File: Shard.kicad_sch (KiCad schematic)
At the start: 43 parts, among them J1 USB_C_Receptacle_USB2.0_16P, J2 Conn_01x02_Pin, SW1 SW_Push, SW2 SW_Push, U1 ESP32-S3, U2 USBLC6-2P6, U3 TLV76733DRVx, U4 TLV76733DRVx, U5 W25Q128JVS, Y1 Crystal_GND24_Small

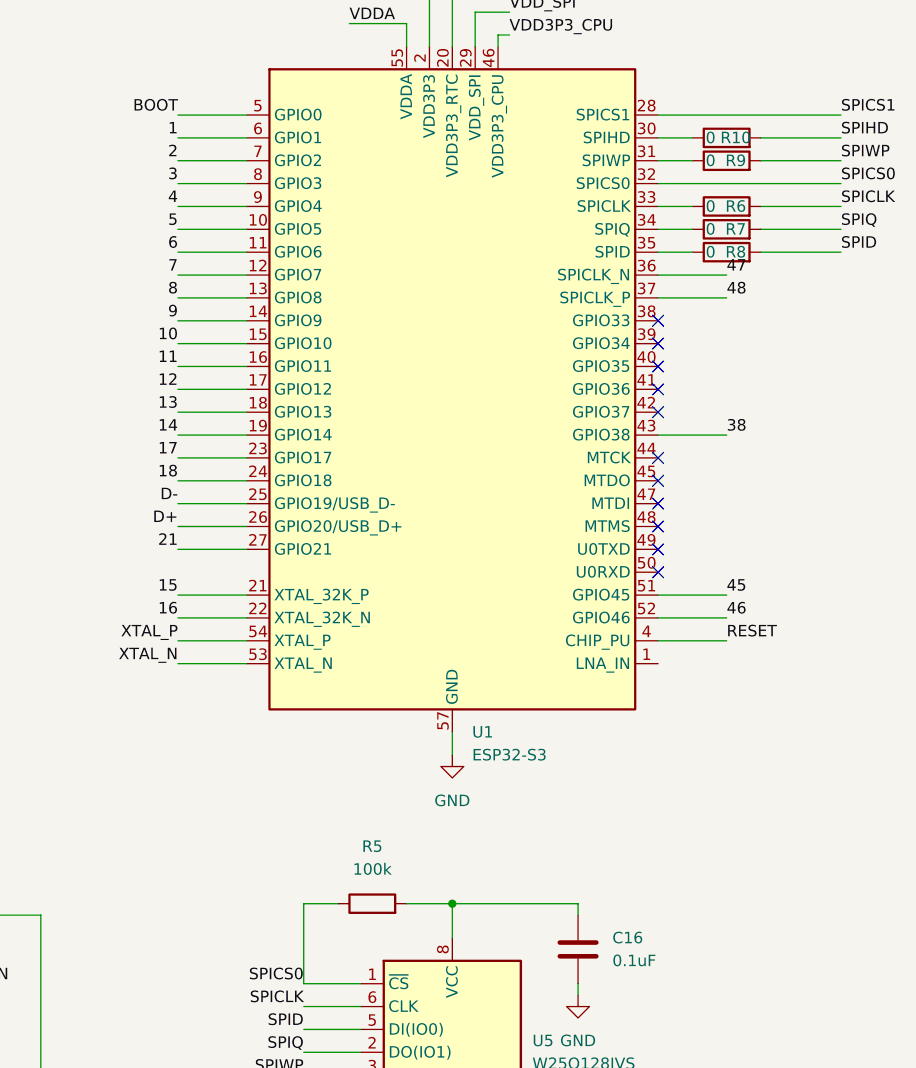
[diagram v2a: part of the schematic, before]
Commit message: GPIO pin labeling
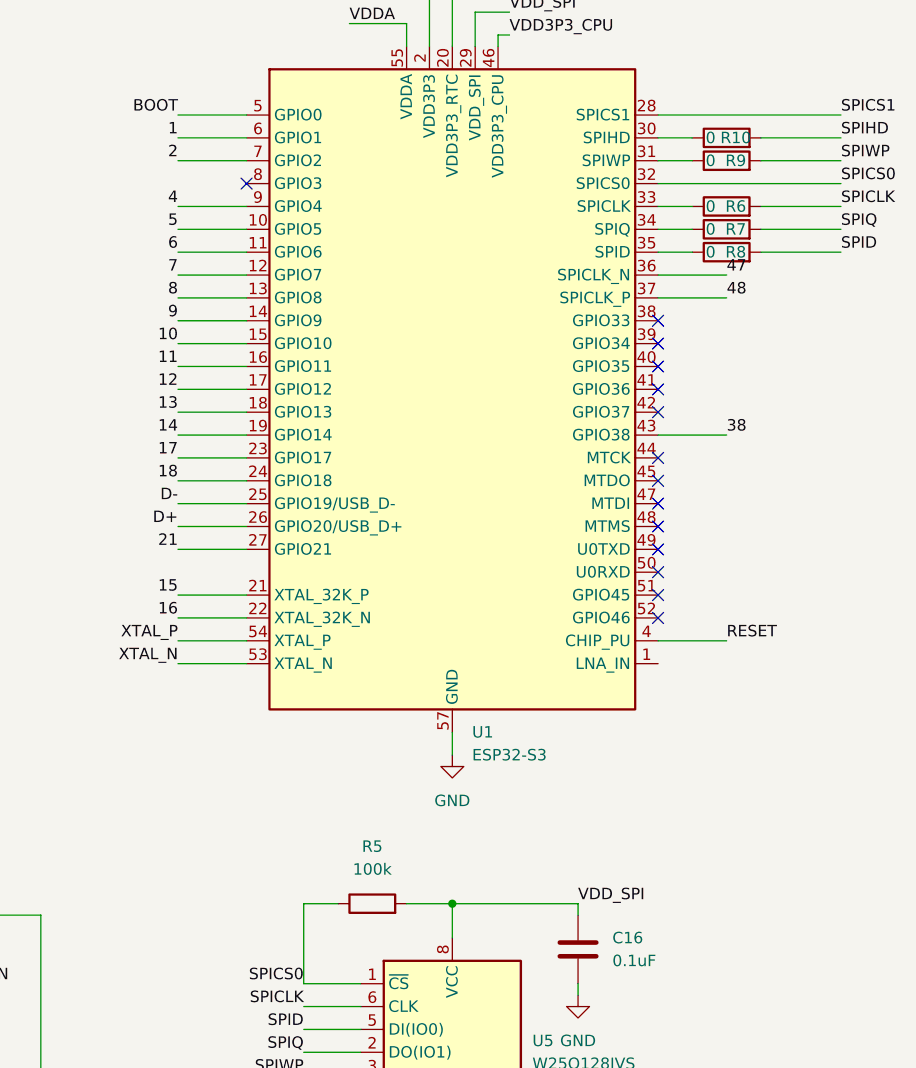
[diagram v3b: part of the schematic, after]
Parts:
- U1: REF C2913192 -> C2913194
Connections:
- net VDD_SPI: now also C16.1, R5.2, U5.8 (VCC)
- net 3: no longer names the net of U1.8 (GPIO3)
- net 45: no longer names the net of U1.51 (GPIO45)
- net 46: no longer names the net of U1.52 (GPIO46)
- no-connect marks 14 -> 17
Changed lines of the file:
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@@
 	)
 	(no_connect
+		(at 359.41 105.41)
+	)
+	(no_connect
+		(at 359.41 107.95)
+	)
+	(no_connect
 		(at 359.41 74.93)
 	)
@@
 	)
 	(no_connect
+		(at 313.69 59.69)
+	)
+	(no_connect
 		(at 49.53 97.79)
 	)
@@
 	(wire
 		(pts
-			(xy 359.41 105.41) (xy 367.03 105.41)
-		)
-		(stroke
-			(width 0)
-			(type default)
-		)
-	)
-	(wire
-		(pts
 			(xy 44.45 190.5) (xy 44.45 191.77)
 		)
@@
 	(wire
 		(pts
-			(xy 359.41 107.95) (xy 367.03 107.95)
-		)
-		(stroke
-			(width 0)
-			(type default)
-		)
-	)
-	(wire
-		(pts
 			(xy 67.31 165.1) (xy 67.31 166.37)
 		)
@@
 	(wire
 		(pts
-			(xy 306.07 59.69) (xy 313.69 59.69)
-		)
-		(stroke
-			(width 0)
-			(type default)
-		)
-	)
-	(wire
-		(pts
 			(xy 137.16 33.02) (xy 144.78 33.02)
 		)
@@
 		)
 	)
-	(label "3"
-		(at 306.07 59.69 180)
+	(label "VDD_SPI"
+		(at 350.52 139.7 0)
 		(fields_autoplaced yes)
 		(effects
@@
 				(size 1.27 1.27)
 			)
-			(justify right bottom)
+			(justify left bottom)
 		)
 	)
@@
 		)
 	)
-	(label "46"
-		(at 367.03 107.95 0)
-		(fields_autoplaced yes)
-		(effects
-			(font
-				(size 1.27 1.27)
-			)
-			(justify left bottom)
-		)
-	)
 	(label "10"
 		(at 306.07 77.47 180)
@@
 		)
 	)
-	(label "45"
-		(at 367.03 105.41 0)
-		(fields_autoplaced yes)
-		(effects
-			(font
-				(size 1.27 1.27)
-			)
-			(justify left bottom)
-		)
-	)
 	(label "SPICS0"
 		(at 379.73 59.69 0)
@@
 			)
 		)
-		(property "REF" "C2913192"
+		(property "REF" "C2913194"
 			(at 336.55 82.55 0)
 			(effects

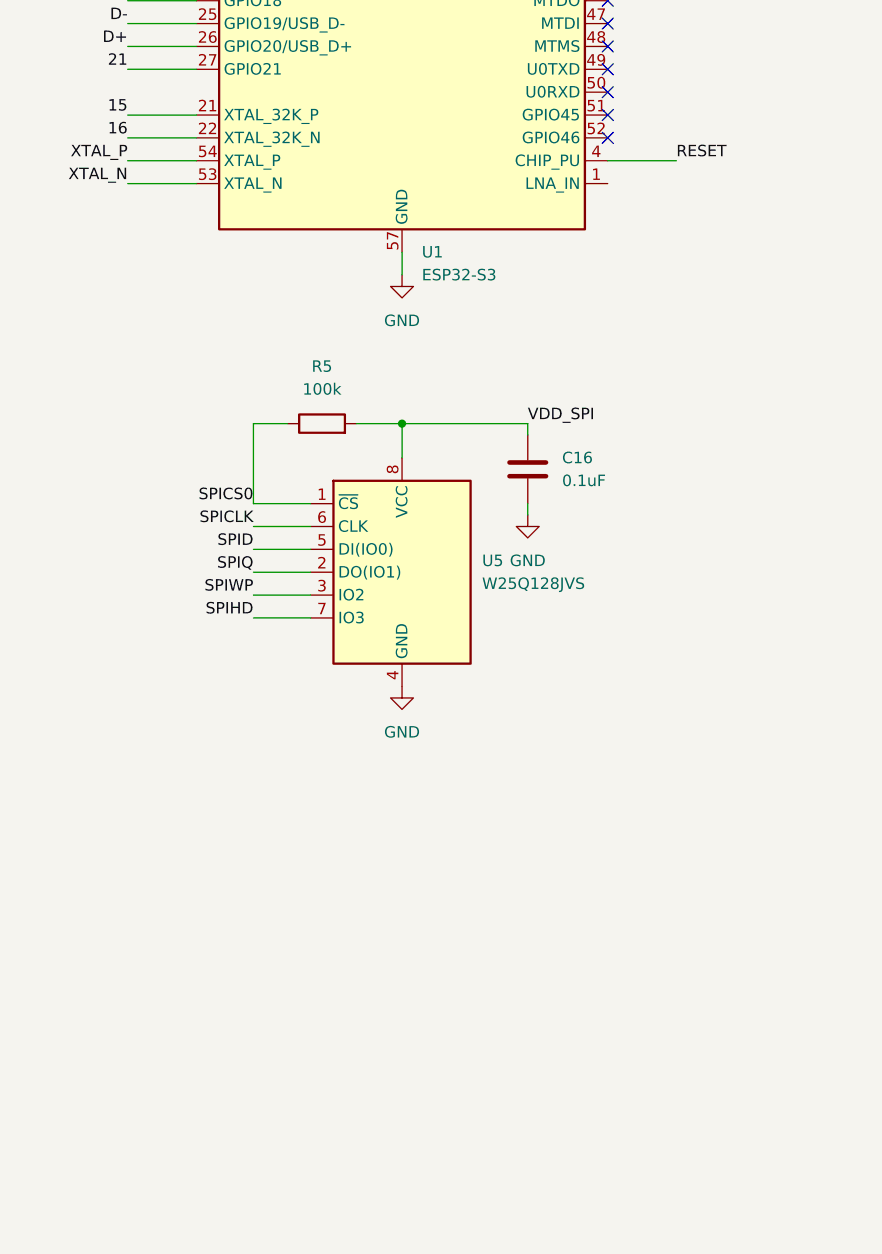
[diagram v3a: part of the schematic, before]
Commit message: Add RF circuit
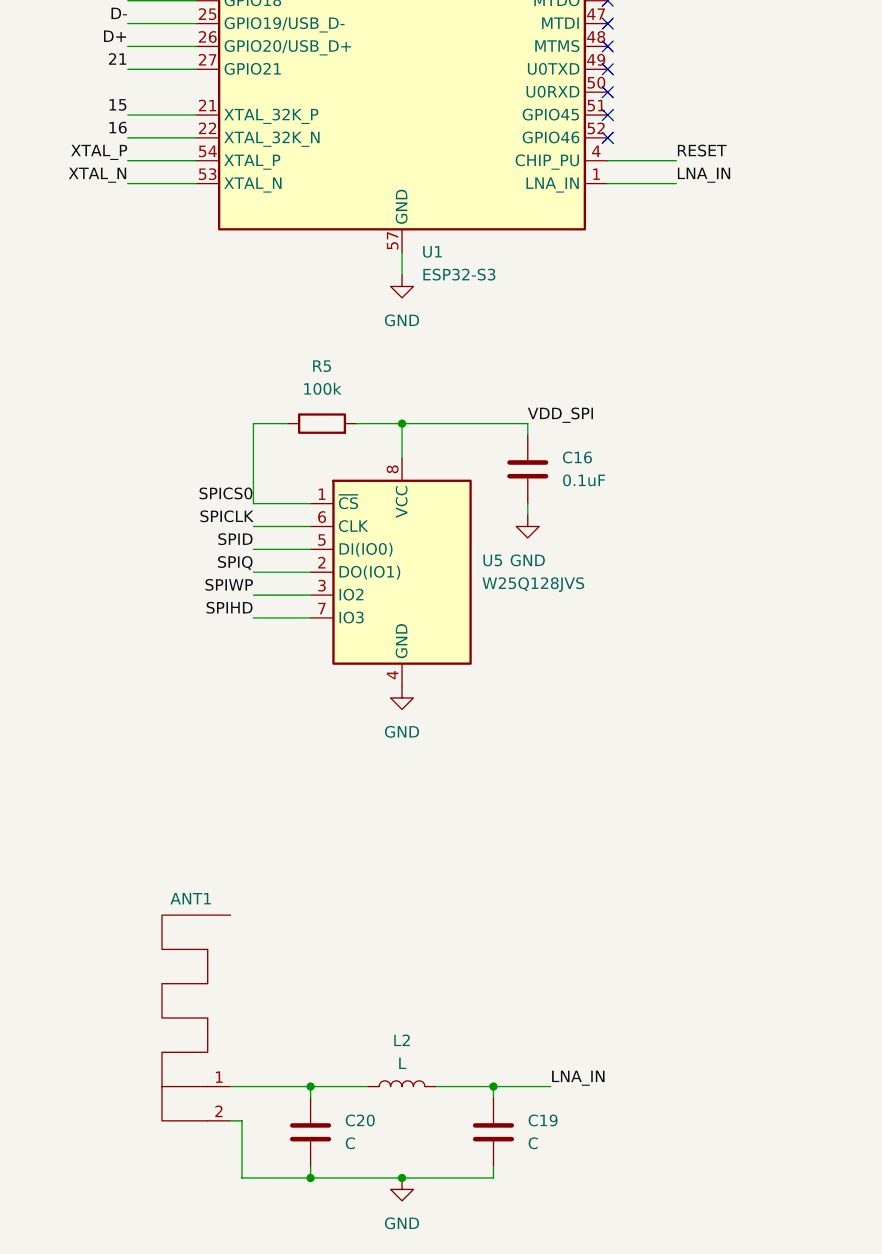
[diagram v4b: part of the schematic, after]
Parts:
- added ANT1: ~, symbol Shard_symlib:RF_ANTENNA
- added C19, C20: C, symbol Device:C
- added L2: L, symbol Device:L
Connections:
- net GND: now also ANT1.2, C19.2, C20.2
- net LNA_IN: now reaches U1.1 (LNA_IN)
- net LNA_IN: now also C19.1, L2.2
- new net: ANT1.1, C20.1, L2.1

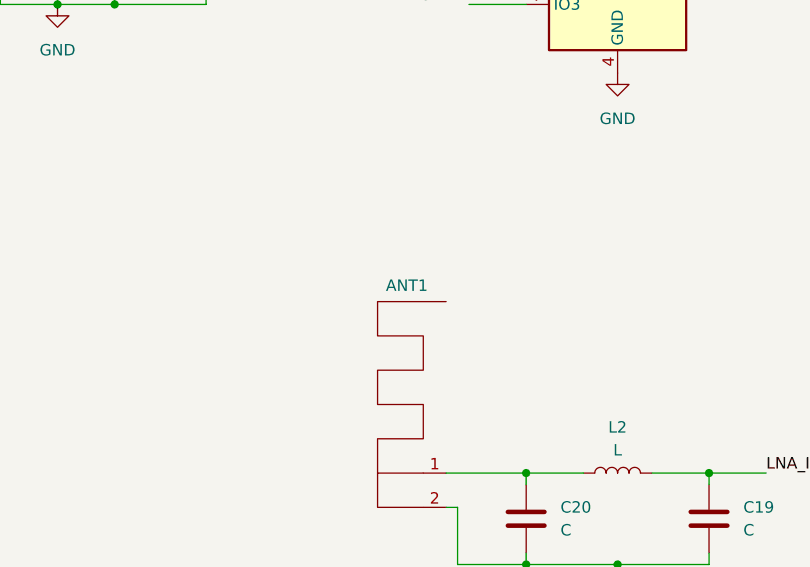
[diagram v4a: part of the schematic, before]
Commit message: Add RF Antenna footprint
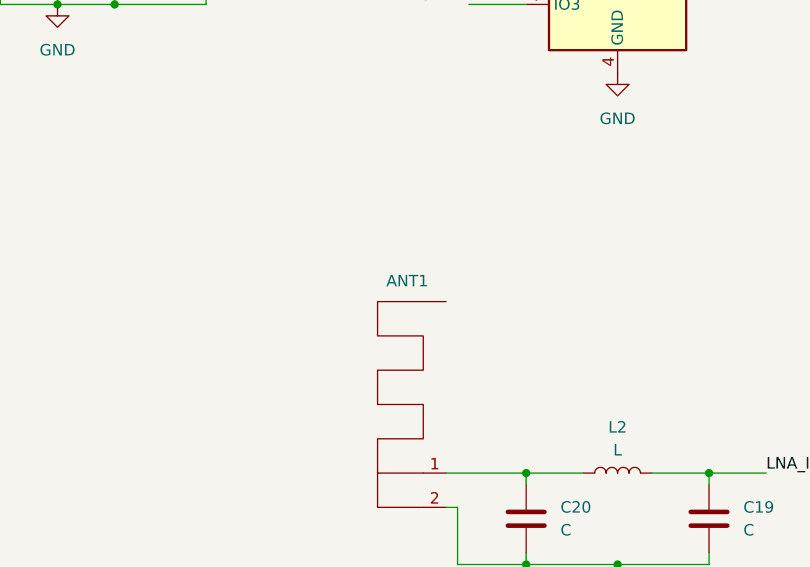
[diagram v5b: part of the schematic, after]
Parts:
- ANT1: footprint (none) -> RF_Antenna:Texas_SWRA117D_2.4GHz_Left
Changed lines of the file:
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@@
 	)
 	(symbol
-		(lib_id "Shard_symlib:RF_ANTENNA")
-		(at 314.96 207.01 0)
-		(mirror y)
-		(unit 1)
-		(exclude_from_sim no)
-		(in_bom yes)
-		(on_board yes)
-		(dnp no)
-		(property "Reference" "ANT1"
-			(at 315.468 192.532 0)
-			(effects
-				(font
-					(size 1.27 1.27)
-				)
-				(justify left)
-			)
-		)
-		(property "Value" "~"
-			(at 308.61 207.01 0)
-			(effects
-				(font
-					(size 1.27 1.27)
-				)
-				(justify left)
-			)
-		)
-		(property "Footprint" ""
-			(at 314.96 207.01 0)
-			(effects
-				(font
-					(size 1.27 1.27)
-				)
-				(hide yes)
-			)
-		)
-		(property "Datasheet" ""
-			(at 314.96 207.01 0)
-			(effects
-				(font
-					(size 1.27 1.27)
-				)
-				(hide yes)
-			)
-		)
-		(property "Description" ""
-			(at 314.96 207.01 0)
-			(effects
-				(font
-					(size 1.27 1.27)
-				)
-				(hide yes)
-			)
-		)
-		(pin "1"
-		)
-		(pin "2"
-		)
-		(instances
-			(project ""
-				(path "/3c105ee6-b3fb-4e5c-8d42-ae0480f22c07"
-					(reference "ANT1")
-					(unit 1)
-				)
-			)
-		)
-	)
-	(symbol
 		(lib_id "power:VBUS")
 		(at 53.34 67.31 0)
@@
 					(unit 1)
 				)
+			)
+		)
+	)
+	(symbol
+		(lib_id "Shard_symlib:RF_ANTENNA")
+		(at 314.96 207.01 0)
+		(mirror y)
+		(unit 1)
+		(exclude_from_sim no)
+		(in_bom yes)
+		(on_board yes)
+		(dnp no)
+		(property "Reference" "ANT1"
+			(at 313.182 192.024 0)
+			(effects
+				(font
+					(size 1.27 1.27)
+				)
+			)
+		)
+		(property "Value" "~"
+			(at 313.69 193.04 0)
+			(effects
+				(font
+					(size 1.27 1.27)
+				)
+			)
+		)
+		(property "Footprint" "RF_Antenna:Texas_SWRA117D_2.4GHz_Left"
+			(at 314.96 207.01 0)
+			(effects
+				(font
+					(size 1.27 1.27)
+				)
+				(hide yes)
+			)
+		)
+		(property "Datasheet" ""
+			(at 314.96 207.01 0)
+			(effects
+				(font
+					(size 1.27 1.27)
+				)
+				(hide yes)
+			)
+		)
+		(property "Description" ""
+			(at 314.96 207.01 0)
+			(effects
+				(font
+					(size 1.27 1.27)
+				)
+				(hide yes)
+			)
+		)
+		(pin "1"
+		)
+		(pin "2"
+		)
+		(instances
+			(project ""
+				(path "/3c105ee6-b3fb-4e5c-8d42-ae0480f22c07"
+					(reference "ANT1")
+					(unit 1)
+				)

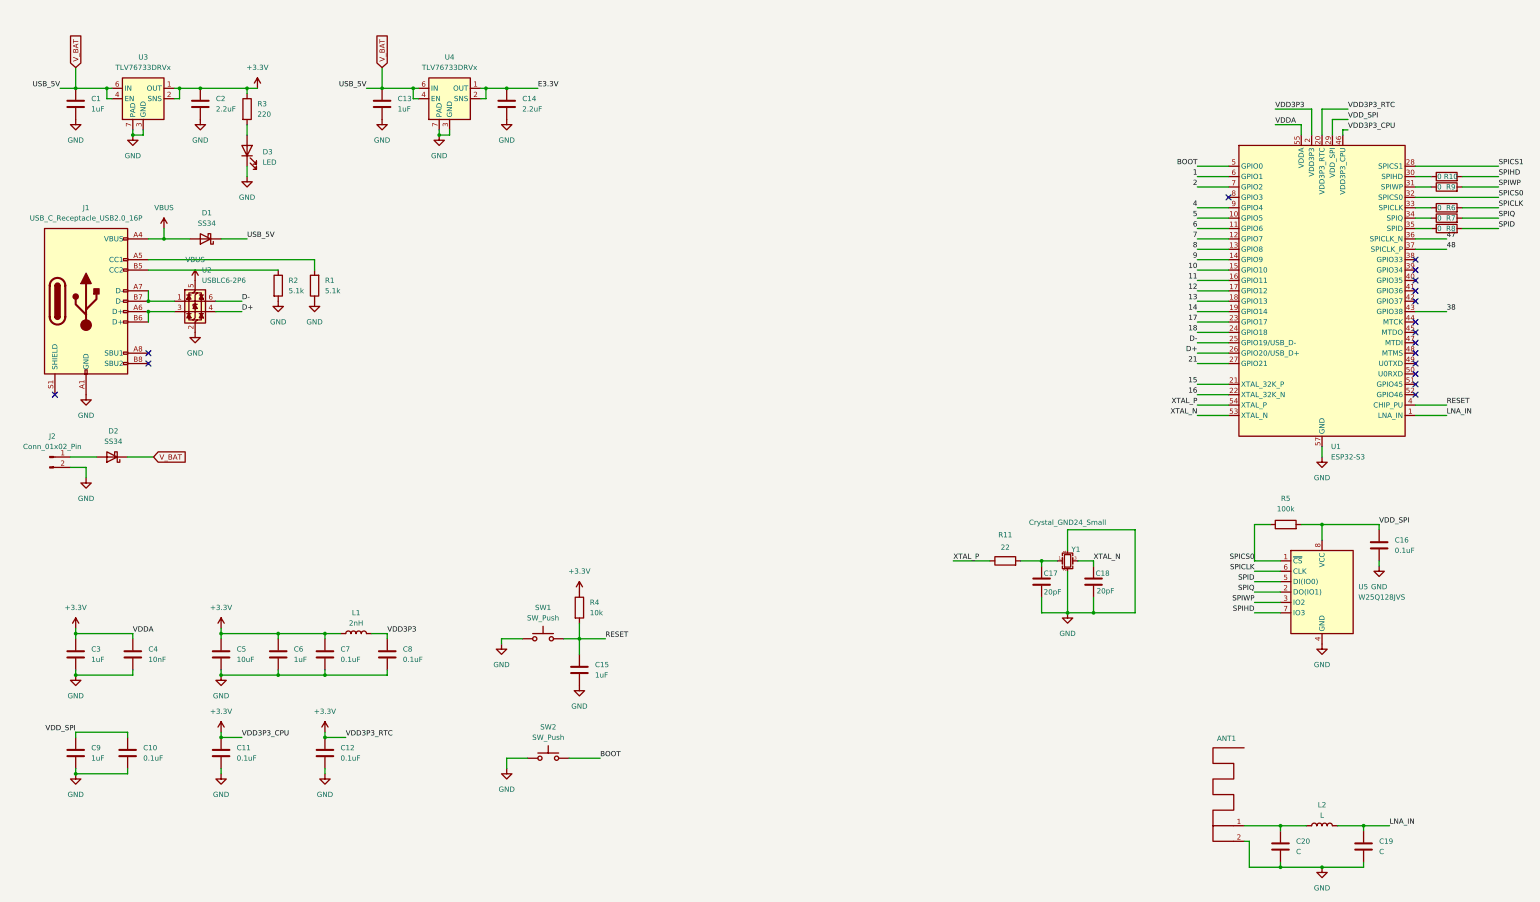
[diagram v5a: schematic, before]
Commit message: Finished schematic with headers
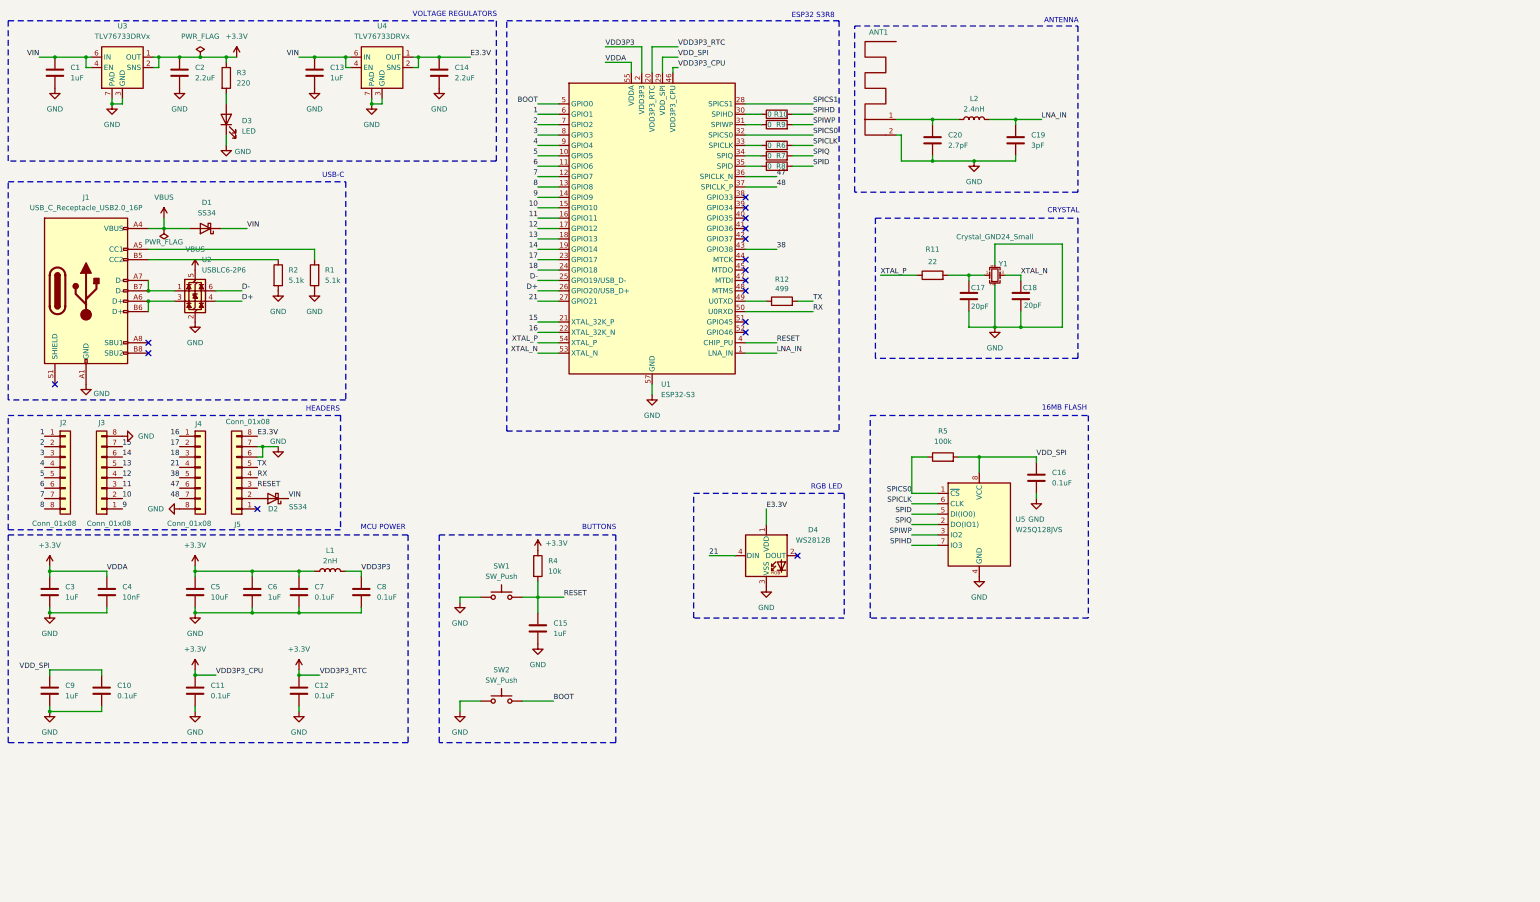
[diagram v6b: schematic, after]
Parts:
- removed J2: Conn_01x02_Pin, symbol Connector:Conn_01x02_Pin
- added D4: WS2812B, LED_SMD:LED_WS2812B_PLCC4_5.0x5.0mm_P3.2mm, symbol LED:WS2812B
- added J2, J3, J4, J5: Conn_01x08, symbol Connector_Generic:Conn_01x08
- added R12: 499, Resistor_SMD:R_0805_2012Metric, symbol Device:R
- C19: value C -> 3pF; footprint (none) -> Capacitor_SMD:C_0201_0603Metric; REF (none) -> C508850
- C20: value C -> 2.7pF; footprint (none) -> Capacitor_SMD:C_0402_1005Metric; REF (none) -> C386137
- L2: value L -> 2.4nH; footprint (none) -> Inductor_SMD:L_0201_0603Metric; REF (none) -> C87200
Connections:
- net 1: now also J2.1 (Pin_1)
- net 10: now also J3.2 (Pin_2)
- net 11: now also J3.3 (Pin_3)
- net 12: now also J3.4 (Pin_4)
- net 13: now also J3.5 (Pin_5)
- net 14: now also J3.6 (Pin_6)
- net 15: now also J3.7 (Pin_7)
- net 16: now also J4.1 (Pin_1)
- net 17: now also J4.2 (Pin_2)
- net 18: now also J4.3 (Pin_3)
- net 2: now also J2.2 (Pin_2)
- net 21: now also D4.4 (DIN), J4.4 (Pin_4)
- net 38: now also J4.5 (Pin_5)
- net 4: now also J2.4 (Pin_4)
- net 47: now also J4.6 (Pin_6)
- net 48: now also J4.7 (Pin_7)
- net 5: now also J2.5 (Pin_5)
- net 6: now also J2.6 (Pin_6)
- net 7: now also J2.7 (Pin_7)
- net 8: now also J2.8 (Pin_8)
- net 9: now also J3.1 (Pin_1)
- net E3.3V: now also D4.1 (VDD), J5.8 (Pin_8)
- net GND: now also D4.3 (VSS), J3.8 (Pin_8), J4.8 (Pin_8), J5.6 (Pin_6), J5.7 (Pin_7)
- net RESET: now also J5.3 (Pin_3)
- net at U1.49 (U0TXD): now also R12.1
- net RX: now reaches U1.50 (U0RXD)
- net RX: now also J5.4 (Pin_4)
- net 3: now reaches U1.8 (GPIO3)
- net 3: now also J2.3 (Pin_3)
- net at D2.2 (A): now also J5.2 (Pin_2)
- net V_BAT renamed VIN
- new net TX: J5.5 (Pin_5), R12.2
- no-connect marks 17 -> 16
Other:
- note added: "16MB FLASH"
- note added: "ANTENNA"
- note added: "BUTTONS"
- note added: "CRYSTAL"
- note added: "ESP32 S3R8"
- note added: "HEADERS"
- note added: "MCU POWER"
- note added: "RGB LED"
- note added: "USB-C"
- note added: "VOLTAGE REGULATORS"
- moved on the sheet: ANT1, C1, C10, C11, C12, C13, C14, C15, C16, C17, C18, C19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
